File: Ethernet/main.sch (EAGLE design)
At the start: 35 parts, among them J1 J00-0045NL, P1 LAN8742A-CZ

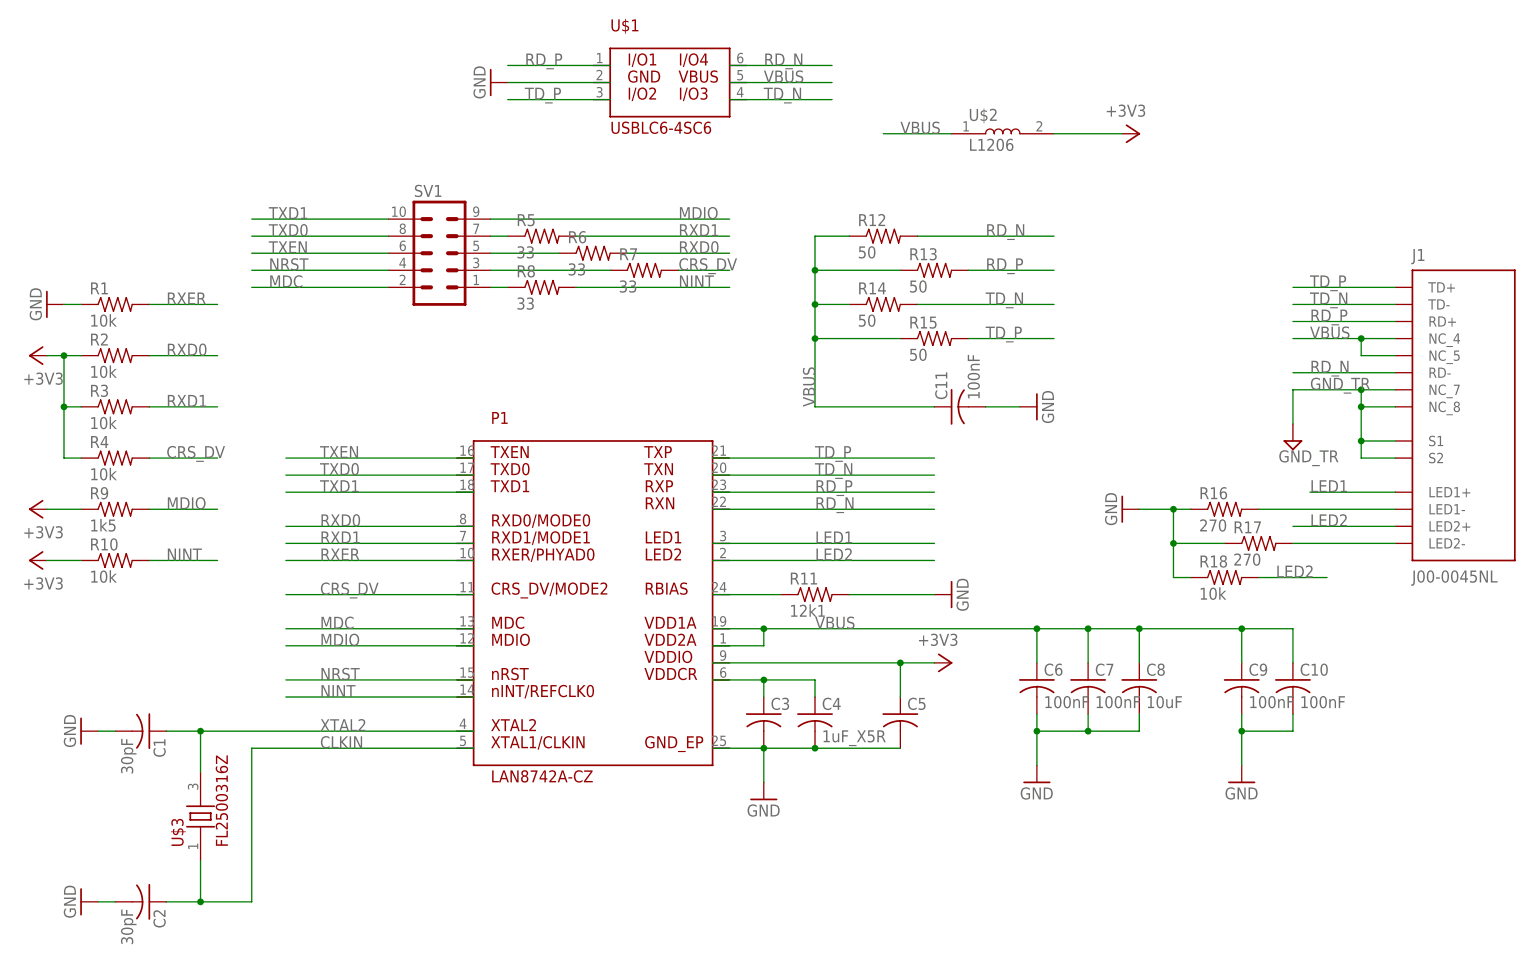
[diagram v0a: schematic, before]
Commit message: Ethernet PCB finalized
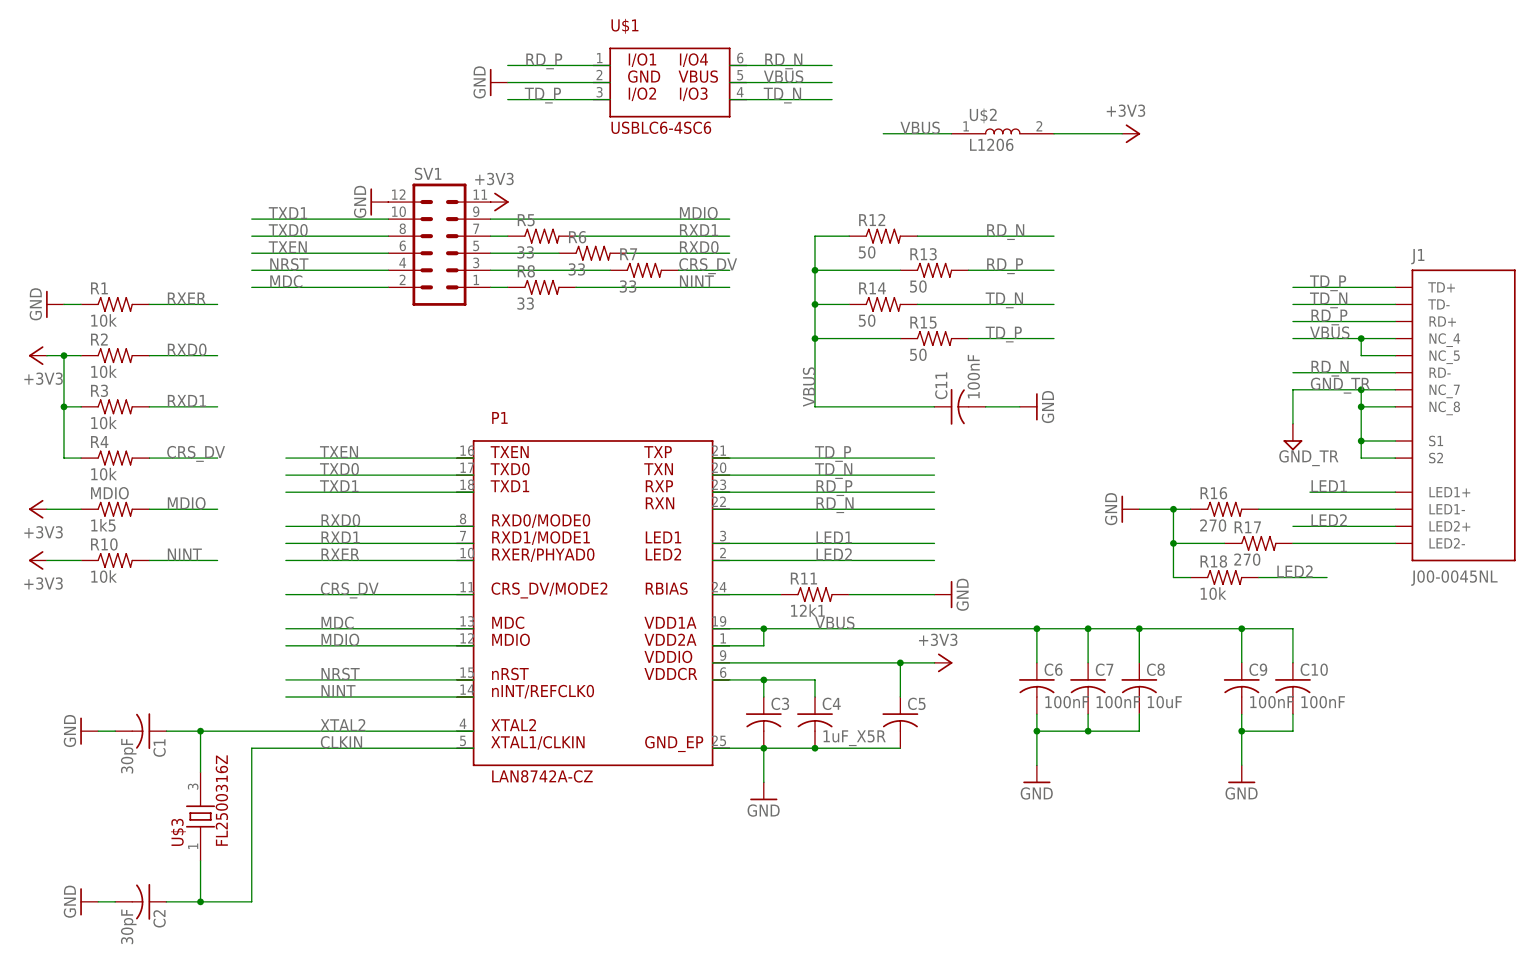
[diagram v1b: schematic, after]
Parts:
- SV1: device con-lstb:MA05-2 -> con-lstb:MA06-2
- renumbered R9 to MDIO
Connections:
- net +3V3: now also SV1.11
- net GND: now also SV1.12
